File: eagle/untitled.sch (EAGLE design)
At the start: 38 parts, among them J1 JTAG, U1 MMA3202KEG

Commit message: Rework some labels.
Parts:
- Q1: value (none) -> 16MHz
- S1: value TAC_SWITCHSMD -> RESET
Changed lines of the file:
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@@
 <part name="R1" library="SparkFun-Passives" deviceset="RESISTOR" device="1206"/>
 <part name="R2" library="SparkFun-Passives" deviceset="RESISTOR" device="1206"/>
-<part name="S1" library="SparkFun-Retired" deviceset="TAC_SWITCH" device="SMD" value="TAC_SWITCHSMD"/>
+<part name="S1" library="SparkFun-Retired" deviceset="TAC_SWITCH" device="SMD" value="RESET"/>
 <part name="R3" library="SparkFun-Passives" deviceset="RESISTOR" device="1206" value="10k"/>
 <part name="GND-ISO1" library="SparkFun-Aesthetics" deviceset="GND-ISO" device=""/>
 <part name="GND-ISO2" library="SparkFun-Aesthetics" deviceset="GND-ISO" device=""/>
-<part name="Q1" library="special" deviceset="XTAL/S" device=""/>
+<part name="Q1" library="special" deviceset="XTAL/S" device="" value="16MHz"/>
 <part name="C1" library="capacitor-wima" deviceset="C" device="2.5/2"/>
 <part name="C2" library="capacitor-wima" deviceset="C" device="2.5/2"/>

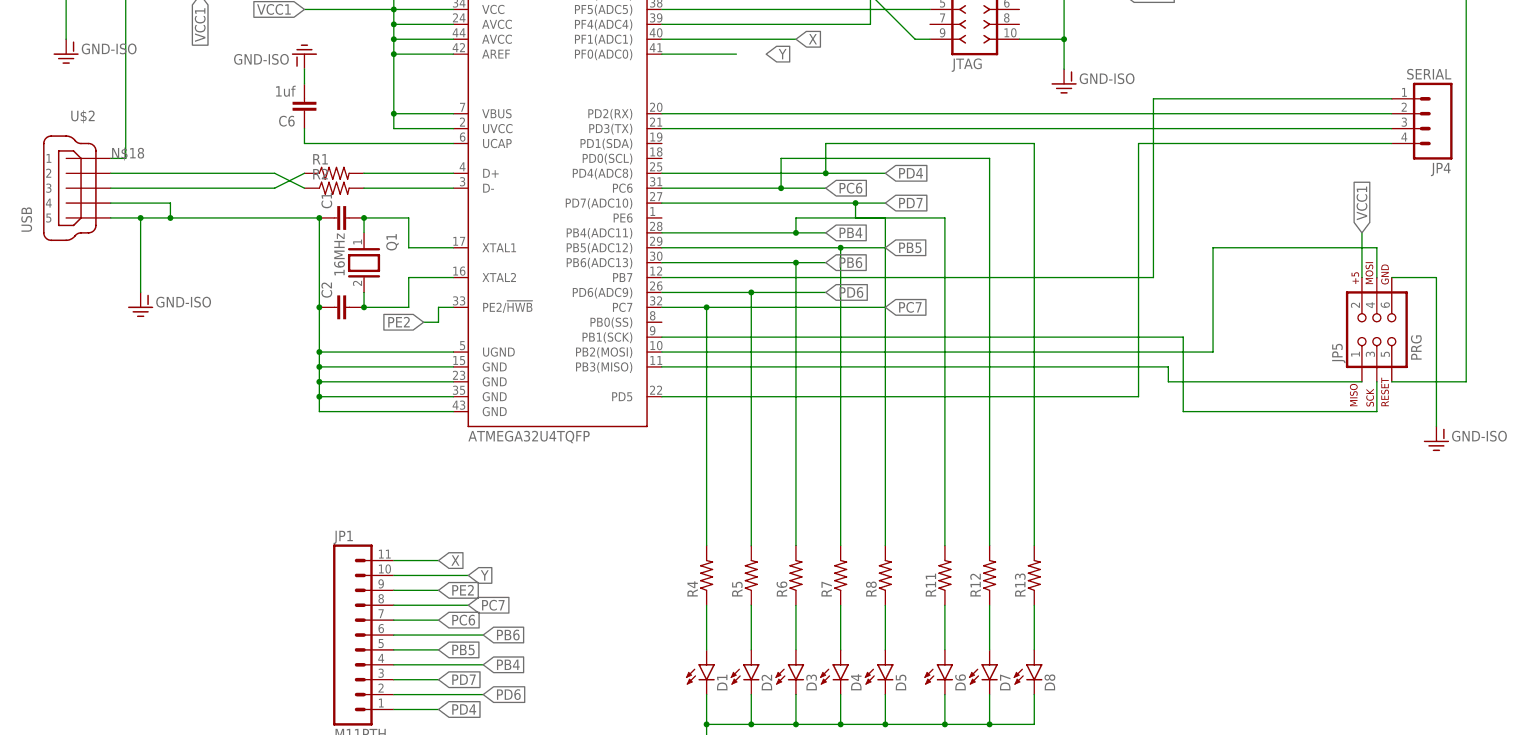
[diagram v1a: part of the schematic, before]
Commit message: Replace usb micro connector with mini type.
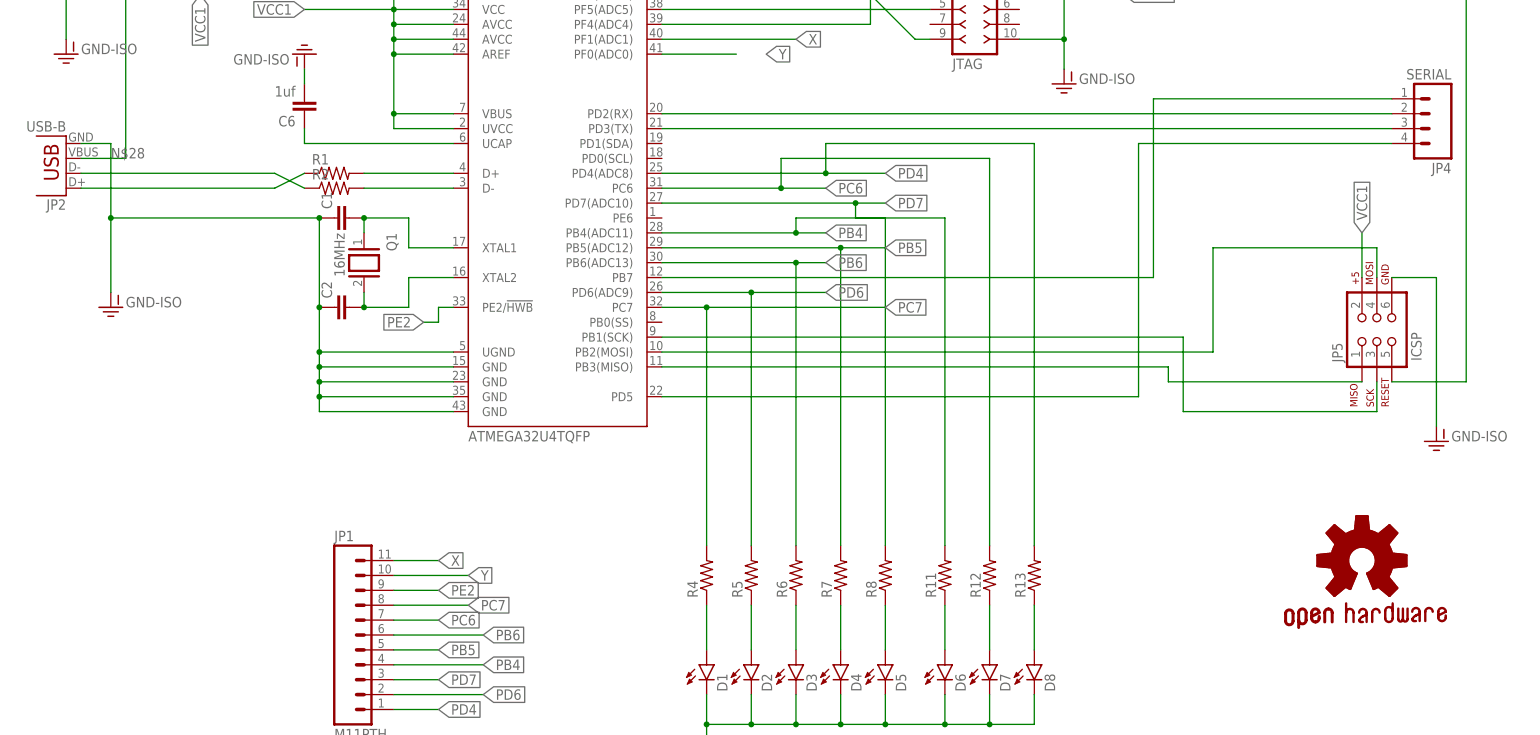
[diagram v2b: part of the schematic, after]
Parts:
- removed U$2: USB, con-hirose:MICRO-USB-ZX62R-B-5P
- added GOLD_ORB_SM1: OSHWLOGO_GOLD_ORB_SM, bfl:OSHWLOGO_GOLD_ORB_SM
- added JP2: USB-B, SparkFun-Connectors:USBPTH
- C6: device capacitor-wima:C2.5/2 -> eagle-ltspice:CC1206
- JP5: value PRG -> ICSP
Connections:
- removed net N$18: G1.+, SJ1.2, U$2.1
- new net N$28: G1.+, JP2.VBUS, SJ1.2
- net GND-ISO: now also JP2.GND; no longer U$2.4, U$2.5
- net N$3: now also JP2.D-; no longer U$2.2
- net N$4: now also JP2.D+; no longer U$2.3
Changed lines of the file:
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@@
 <parts>
 <part name="U$1" library="SparkFun-Retired" deviceset="ATMEGA32U4" device="TQFP"/>
-<part name="U$2" library="con-hirose" deviceset="MICRO-USB-" device="ZX62R-B-5P" value="USB"/>
 <part name="R1" library="SparkFun-Passives" deviceset="RESISTOR" device="1206"/>
 <part name="R2" library="SparkFun-Passives" deviceset="RESISTOR" device="1206"/>
@@
 <part name="GND-ISO6" library="SparkFun-Aesthetics" deviceset="GND-ISO" device=""/>
 <part name="GND-ISO7" library="SparkFun-Aesthetics" deviceset="GND-ISO" device=""/>
-<part name="C6" library="capacitor-wima" deviceset="C" device="2.5/2" value="1uf"/>
+<part name="C6" library="eagle-ltspice" deviceset="C" device="C1206" value="1uf"/>
 <part name="GND-ISO8" library="SparkFun-Aesthetics" deviceset="GND-ISO" device=""/>
 <part name="JP4" library="SparkFun-Connectors" deviceset="M04" device="LOCK_LONGPADS" value="SERIAL"/>
-<part name="JP5" library="SparkFun-Connectors" deviceset="AVR_SPI_PRG_6" device="PTH" value="PRG"/>
+<part name="JP5" library="SparkFun-Connectors" deviceset="AVR_SPI_PRG_6" device="PTH" value="ICSP"/>
 <part name="GND-ISO3" library="SparkFun-Aesthetics" deviceset="GND-ISO" device=""/>
 <part name="JP1" library="SparkFun-Connectors" deviceset="M11" device="PTH"/>
@@
 <part name="J1" library="con-headers-jp" deviceset="F-2X05-" device="DIL-2MM" value="JTAG"/>
 <part name="GND-ISO10" library="SparkFun-Aesthetics" deviceset="GND-ISO" device=""/>
+<part name="GOLD_ORB_SM1" library="bfl" deviceset="OSHWLOGO" device="_GOLD_ORB_SM"/>
+<part name="JP2" library="SparkFun-Connectors" deviceset="USB" device="PTH" value="USB-B"/>
 </parts>
 <sheets>
@@
 <instances>
 <instance part="U$1" gate="G$1" x="43.18" y="43.18"/>
-<instance part="U$2" gate="G$1" x="-38.1" y="43.18" rot="MR0"/>
 <instance part="R1" gate="G$1" x="5.08" y="45.72"/>
 <instance part="R2" gate="G$1" x="5.08" y="43.18"/>
@@
 <instance part="R3" gate="G$1" x="15.24" y="83.82" rot="R270"/>
 <instance part="GND-ISO1" gate="G$1" x="-5.08" y="86.36"/>
-<instance part="GND-ISO2" gate="G$1" x="-27.94" y="22.86"/>
+<instance part="GND-ISO2" gate="G$1" x="-33.02" y="22.86"/>
 <instance part="Q1" gate="G$1" x="10.16" y="30.48" rot="R270"/>
 <instance part="C1" gate="G$1" x="5.08" y="38.1" rot="R90"/>
@@
 <instance part="J1" gate="G$1" x="114.3" y="73.66"/>
 <instance part="GND-ISO10" gate="G$1" x="129.54" y="60.96"/>
+<instance part="GOLD_ORB_SM1" gate="G$1" x="180.34" y="-20.32"/>
+<instance part="JP2" gate="G$1" x="-40.64" y="50.8" rot="R180"/>
 </instances>
 <busses>
@@
 <net name="N$3" class="0">
 <segment>
-<pinref part="U$2" gate="G$1" pin="2"/>
-<wire x1="-33.02" y1="45.72" x2="-5.08" y2="45.72" width="0.1524" layer="91"/>
+<wire x1="-38.1" y1="45.72" x2="-5.08" y2="45.72" width="0.1524" layer="91"/>
 <wire x1="-5.08" y1="45.72" x2="0" y2="43.18" width="0.1524" layer="91"/>
 <pinref part="R2" gate="G$1" pin="1"/>
+<pinref part="JP2" gate="G$1" pin="D-"/>
 </segment>
 </net>
 <net name="N$4" class="0">
 <segment>
-<pinref part="U$2" gate="G$1" pin="3"/>
-<wire x1="-33.02" y1="43.18" x2="-5.08" y2="43.18" width="0.1524" layer="91"/>
+<wire x1="-38.1" y1="43.18" x2="-5.08" y2="43.18" width="0.1524" layer="91"/>
 <wire x1="-5.08" y1="43.18" x2="0" y2="45.72" width="0.1524" layer="91"/>
 <pinref part="R1" gate="G$1" pin="1"/>
+<pinref part="JP2" gate="G$1" pin="D+"/>
 </segment>
 </net>
@@
 </segment>
 <segment>
-<pinref part="U$2" gate="G$1" pin="5"/>
-<wire x1="-33.02" y1="38.1" x2="-27.94" y2="38.1" width="0.1524" layer="91"/>
-<wire x1="-27.94" y1="38.1" x2="-22.86" y2="38.1" width="0.1524" layer="91"/>
-<wire x1="-22.86" y1="38.1" x2="2.54" y2="38.1" width="0.1524" layer="91"/>
+<wire x1="-33.02" y1="38.1" x2="2.54" y2="38.1" width="0.1524" layer="91"/>
 <wire x1="2.54" y1="38.1" x2="2.54" y2="22.86" width="0.1524" layer="91"/>
 <pinref part="U$1" gate="G$1" pin="UGND"/>
 <wire x1="2.54" y1="22.86" x2="2.54" y2="15.24" width="0.1524" layer="91"/>
 <wire x1="2.54" y1="15.24" x2="25.4" y2="15.24" width="0.1524" layer="91"/>
-<pinref part="U$2" gate="G$1" pin="4"/>
-<wire x1="-33.02" y1="40.64" x2="-22.86" y2="40.64" width="0.1524" layer="91"/>
-<wire x1="-22.86" y1="40.64" x2="-22.86" y2="38.1" width="0.1524" layer="91"/>
-<junction x="-22.86" y="38.1"/>
 <pinref part="GND-ISO2" gate="G$1" pin="GND-ISO"/>
-<wire x1="-27.94" y1="25.4" x2="-27.94" y2="38.1" width="0.1524" layer="91"/>
-<junction x="-27.94" y="38.1"/>
+<junction x="-33.02" y="38.1"/>
 <pinref part="U$1" gate="G$1" pin="GND@43"/>
+<wire x1="-33.02" y1="25.4" x2="-33.02" y2="38.1" width="0.1524" layer="91"/>
 <wire x1="25.4" y1="5.08" x2="2.54" y2="5.08" width="0.1524" layer="91"/>
 <wire x1="2.54" y1="5.08" x2="2.54" y2="7.62" width="0.1524" layer="91"/>
@@
 <pinref part="C2" gate="G$1" pin="1"/>
 <junction x="2.54" y="22.86"/>
+<pinref part="JP2" gate="G$1" pin="GND"/>
+<wire x1="-38.1" y1="50.8" x2="-33.02" y2="50.8" width="0.1524" layer="91"/>
+<wire x1="-33.02" y1="50.8" x2="-33.02" y2="38.1" width="0.1524" layer="91"/>
 </segment>
 <segment>
@@
 </segment>
 </net>
-<net name="N$18" class="0">
-<segment>
-<pinref part="U$2" gate="G$1" pin="1"/>
-<wire x1="-33.02" y1="48.26" x2="-30.48" y2="48.26" width="0.1524" layer="91"/>
-<label x="-33.02" y="48.26" size="1.778" layer="95"/>
-<pinref part="SJ1" gate="G$1" pin="2"/>
-<wire x1="-30.48" y1="48.26" x2="-30.48" y2="88.9" width="0.1524" layer="91"/>
-<wire x1="-30.48" y1="88.9" x2="-22.86" y2="88.9" width="0.1524" layer="91"/>
-<pinref part="G1" gate="G$1" pin="+"/>
-<wire x1="-30.48" y1="88.9" x2="-40.64" y2="88.9" width="0.1524" layer="91"/>
-<junction x="-30.48" y="88.9"/>
-</segment>
-</net>
 <net name="VCC1" class="0">
 <segment>
@@
 </segment>
 </net>
+<net name="N$28" class="0">
+<segment>
+<pinref part="G1" gate="G$1" pin="+"/>
+<pinref part="SJ1" gate="G$1" pin="2"/>
+<wire x1="-30.48" y1="88.9" x2="-22.86" y2="88.9" width="0.1524" layer="91"/>
+<wire x1="-30.48" y1="88.9" x2="-40.64" y2="88.9" width="0.1524" layer="91"/>
+<junction x="-30.48" y="88.9"/>
+<wire x1="-30.48" y1="48.26" x2="-30.48" y2="88.9" width="0.1524" layer="91"/>
+<label x="-33.02" y="48.26" size="1.778" layer="95"/>
+<pinref part="JP2" gate="G$1" pin="VBUS"/>
+<wire x1="-30.48" y1="48.26" x2="-38.1" y2="48.26" width="0.1524" layer="91"/>
+</segment>
+</net>

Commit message: Update eagle files.
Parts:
- added D10, D11, D12: DIODE, gipi:DIODE
- C1, C2, C3, C4, C5: device capacitor-wima:C2.5/2 -> SparkFun-Capacitors:CAP1206
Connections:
- new net N$32: D10.A, JP2.VBUS
- new net N$33: D11.A, G1.+
- new net N$34: D12.A, JP5.2
- net N$28: now also D10.C, D11.C; no longer G1.+, JP2.VBUS
- net VCC1: now also D12.C; no longer JP5.2
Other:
- moved on the sheet: C1, C2, C3, C4, C5
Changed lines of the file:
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@@
 <part name="GND-ISO2" library="SparkFun-Aesthetics" deviceset="GND-ISO" device=""/>
 <part name="Q1" library="special" deviceset="XTAL/S" device="" value="16MHz"/>
-<part name="C1" library="capacitor-wima" deviceset="C" device="2.5/2"/>
-<part name="C2" library="capacitor-wima" deviceset="C" device="2.5/2"/>
+<part name="C1" library="SparkFun-Capacitors" deviceset="CAP" device="1206"/>
+<part name="C2" library="SparkFun-Capacitors" deviceset="CAP" device="1206"/>
 <part name="U1" library="gipi" deviceset="MMA3202KEG" device=""/>
 <part name="G1" library="battery" deviceset="10MM_SM_COIN_CELL_CLIP" device="" value="BAT"/>
 <part name="GND-ISO4" library="SparkFun-Aesthetics" deviceset="GND-ISO" device=""/>
-<part name="C3" library="capacitor-wima" deviceset="C" device="2.5/2"/>
+<part name="C3" library="SparkFun-Capacitors" deviceset="CAP" device="1206"/>
 <part name="SJ1" library="SparkFun-Retired" deviceset="SOLDERJUMPER_2WAY" device="PASTE2&amp;3"/>
 <part name="GND-ISO5" library="SparkFun-Aesthetics" deviceset="GND-ISO" device=""/>
 <part name="R9" library="SparkFun-Passives" deviceset="RESISTOR" device="1206" value="10k"/>
 <part name="R10" library="SparkFun-Passives" deviceset="RESISTOR" device="1206" value="10k"/>
-<part name="C4" library="capacitor-wima" deviceset="C" device="2.5/2"/>
-<part name="C5" library="capacitor-wima" deviceset="C" device="2.5/2"/>
+<part name="C4" library="SparkFun-Capacitors" deviceset="CAP" device="1206"/>
+<part name="C5" library="SparkFun-Capacitors" deviceset="CAP" device="1206"/>
 <part name="GND-ISO6" library="SparkFun-Aesthetics" deviceset="GND-ISO" device=""/>
 <part name="GND-ISO7" library="SparkFun-Aesthetics" deviceset="GND-ISO" device=""/>
@@
 <part name="GOLD_ORB_SM1" library="bfl" deviceset="OSHWLOGO" device="_GOLD_ORB_SM"/>
 <part name="JP2" library="SparkFun-Connectors" deviceset="USB" device="PTH" value="USB-B"/>
+<part name="D10" library="gipi" deviceset="DIODE" device=""/>
+<part name="D11" library="gipi" deviceset="DIODE" device=""/>
+<part name="D12" library="gipi" deviceset="DIODE" device=""/>
 </parts>
 <sheets>
@@
 <instance part="GOLD_ORB_SM1" gate="G$1" x="180.34" y="-20.32"/>
 <instance part="JP2" gate="G$1" x="-40.64" y="50.8" rot="R180"/>
+<instance part="D10" gate="G$1" x="-30.48" y="73.66" rot="R90"/>
+<instance part="D11" gate="G$1" x="-35.56" y="88.9"/>
+<instance part="D12" gate="G$1" x="185.42" y="40.64"/>
 </instances>
 <busses>
@@
 </segment>
 <segment>
-<wire x1="-33.02" y1="38.1" x2="2.54" y2="38.1" width="0.1524" layer="91"/>
-<wire x1="2.54" y1="38.1" x2="2.54" y2="22.86" width="0.1524" layer="91"/>
+<wire x1="-33.02" y1="38.1" x2="0" y2="38.1" width="0.1524" layer="91"/>
+<wire x1="0" y1="38.1" x2="0" y2="22.86" width="0.1524" layer="91"/>
 <pinref part="U$1" gate="G$1" pin="UGND"/>
-<wire x1="2.54" y1="22.86" x2="2.54" y2="15.24" width="0.1524" layer="91"/>
+<wire x1="0" y1="22.86" x2="2.54" y2="15.24" width="0.1524" layer="91"/>
 <wire x1="2.54" y1="15.24" x2="25.4" y2="15.24" width="0.1524" layer="91"/>
 <pinref part="GND-ISO2" gate="G$1" pin="GND-ISO"/>
@@
 <junction x="2.54" y="7.62"/>
 <pinref part="C1" gate="G$1" pin="1"/>
-<junction x="2.54" y="38.1"/>
+<junction x="0" y="38.1"/>
 <pinref part="C2" gate="G$1" pin="1"/>
-<junction x="2.54" y="22.86"/>
+<junction x="0" y="22.86"/>
 <pinref part="JP2" gate="G$1" pin="GND"/>
 <wire x1="-38.1" y1="50.8" x2="-33.02" y2="50.8" width="0.1524" layer="91"/>
@@
 <pinref part="C5" gate="G$1" pin="1"/>
 <pinref part="GND-ISO6" gate="G$1" pin="GND-ISO"/>
+<wire x1="116.84" y1="-157.48" x2="116.84" y2="-160.02" width="0.1524" layer="91"/>
 </segment>
 <segment>
 <pinref part="C4" gate="G$1" pin="1"/>
 <pinref part="GND-ISO7" gate="G$1" pin="GND-ISO"/>
+<wire x1="137.16" y1="-157.48" x2="137.16" y2="-160.02" width="0.1524" layer="91"/>
 </segment>
 <segment>
@@
 <junction x="38.1" y="-149.86"/>
 <wire x1="38.1" y1="-149.86" x2="20.32" y2="-149.86" width="0.1524" layer="91"/>
-<wire x1="20.32" y1="-149.86" x2="20.32" y2="-147.32" width="0.1524" layer="91"/>
 <pinref part="GND-ISO4" gate="G$1" pin="GND-ISO"/>
 <wire x1="38.1" y1="-187.96" x2="38.1" y2="-154.94" width="0.1524" layer="91"/>
@@
 <pinref part="Q1" gate="G$1" pin="2"/>
 <pinref part="C2" gate="G$1" pin="2"/>
-<wire x1="10.16" y1="25.4" x2="10.16" y2="22.86" width="0.1524" layer="91"/>
+<wire x1="10.16" y1="25.4" x2="7.62" y2="22.86" width="0.1524" layer="91"/>
 <wire x1="17.78" y1="27.94" x2="17.78" y2="22.86" width="0.1524" layer="91"/>
-<wire x1="17.78" y1="22.86" x2="10.16" y2="22.86" width="0.1524" layer="91"/>
-<junction x="10.16" y="22.86"/>
+<wire x1="17.78" y1="22.86" x2="7.62" y2="22.86" width="0.1524" layer="91"/>
+<junction x="7.62" y="22.86"/>
 </segment>
 </net>
@@
 <segment>
 <pinref part="C1" gate="G$1" pin="2"/>
-<wire x1="10.16" y1="38.1" x2="17.78" y2="38.1" width="0.1524" layer="91"/>
+<wire x1="7.62" y1="38.1" x2="17.78" y2="38.1" width="0.1524" layer="91"/>
 <wire x1="17.78" y1="38.1" x2="17.78" y2="33.02" width="0.1524" layer="91"/>
 <pinref part="U$1" gate="G$1" pin="XTAL1"/>
 <wire x1="25.4" y1="33.02" x2="17.78" y2="33.02" width="0.1524" layer="91"/>
 <pinref part="Q1" gate="G$1" pin="1"/>
-<wire x1="10.16" y1="38.1" x2="10.16" y2="35.56" width="0.1524" layer="91"/>
-<junction x="10.16" y="38.1"/>
+<wire x1="7.62" y1="38.1" x2="10.16" y2="35.56" width="0.1524" layer="91"/>
+<junction x="7.62" y="38.1"/>
 </segment>
 </net>
@@
 </segment>
 <segment>
-<pinref part="JP5" gate="G$1" pin="2"/>
-<wire x1="180.34" y1="27.94" x2="180.34" y2="35.56" width="0.1524" layer="91"/>
-<label x="180.34" y="35.56" size="1.778" layer="95" rot="R90" xref="yes"/>
-</segment>
-<segment>
 <pinref part="J1" gate="G$1" pin="4"/>
 <wire x1="121.92" y1="76.2" x2="139.7" y2="76.2" width="0.1524" layer="91"/>
 <label x="139.7" y="76.2" size="1.778" layer="95" xref="yes"/>
 </segment>
+<segment>
+<pinref part="D12" gate="G$1" pin="C"/>
+<wire x1="187.96" y1="40.64" x2="203.2" y2="40.64" width="0.1524" layer="91"/>
+<label x="203.2" y="40.64" size="1.778" layer="95" xref="yes"/>
+</segment>
 </net>
 <net name="VCC2" class="0">
@@
 <pinref part="U1" gate="G$1" pin="VCC"/>
 <wire x1="48.26" y1="-139.7" x2="35.56" y2="-139.7" width="0.1524" layer="91"/>
-<wire x1="35.56" y1="-139.7" x2="20.32" y2="-139.7" width="0.1524" layer="91"/>
-<wire x1="20.32" y1="-139.7" x2="20.32" y2="-129.54" width="0.1524" layer="91"/>
+<wire x1="35.56" y1="-139.7" x2="20.32" y2="-142.24" width="0.1524" layer="91"/>
+<wire x1="20.32" y1="-142.24" x2="20.32" y2="-129.54" width="0.1524" layer="91"/>
 <pinref part="C3" gate="G$1" pin="2"/>
-<junction x="20.32" y="-139.7"/>
+<junction x="20.32" y="-142.24"/>
 <label x="20.32" y="-129.54" size="1.778" layer="95" rot="R90" xref="yes"/>
 <pinref part="U1" gate="G$1" pin="AVCC"/>
@@
 <wire x1="106.68" y1="-144.78" x2="137.16" y2="-144.78" width="0.1524" layer="91"/>
 <pinref part="C4" gate="G$1" pin="2"/>
-<wire x1="137.16" y1="-144.78" x2="137.16" y2="-149.86" width="0.1524" layer="91"/>
+<wire x1="137.16" y1="-144.78" x2="137.16" y2="-152.4" width="0.1524" layer="91"/>
 <wire x1="137.16" y1="-144.78" x2="144.78" y2="-144.78" width="0.1524" layer="91"/>
 <junction x="137.16" y="-144.78"/>
@@
 <wire x1="106.68" y1="-139.7" x2="116.84" y2="-139.7" width="0.1524" layer="91"/>
 <pinref part="C5" gate="G$1" pin="2"/>
-<wire x1="116.84" y1="-139.7" x2="116.84" y2="-149.86" width="0.1524" layer="91"/>
+<wire x1="116.84" y1="-139.7" x2="116.84" y2="-152.4" width="0.1524" layer="91"/>
 <junction x="116.84" y="-139.7"/>
 <wire x1="116.84" y1="-139.7" x2="144.78" y2="-139.7" width="0.1524" layer="91"/>
@@
 <net name="N$28" class="0">
 <segment>
-<pinref part="G1" gate="G$1" pin="+"/>
 <pinref part="SJ1" gate="G$1" pin="2"/>
-<wire x1="-30.48" y1="88.9" x2="-22.86" y2="88.9" width="0.1524" layer="91"/>
-<wire x1="-30.48" y1="88.9" x2="-40.64" y2="88.9" width="0.1524" layer="91"/>
+<wire x1="-22.86" y1="88.9" x2="-30.48" y2="88.9" width="0.1524" layer="91"/>
+<pinref part="D10" gate="G$1" pin="C"/>
+<wire x1="-30.48" y1="76.2" x2="-30.48" y2="88.9" width="0.1524" layer="91"/>
+<pinref part="D11" gate="G$1" pin="C"/>
+<wire x1="-33.02" y1="88.9" x2="-30.48" y2="88.9" width="0.1524" layer="91"/>
 <junction x="-30.48" y="88.9"/>
-<wire x1="-30.48" y1="48.26" x2="-30.48" y2="88.9" width="0.1524" layer="91"/>
-<label x="-33.02" y="48.26" size="1.778" layer="95"/>
+</segment>
+</net>
+<net name="N$32" class="0">
+<segment>
 <pinref part="JP2" gate="G$1" pin="VBUS"/>
 <wire x1="-30.48" y1="48.26" x2="-38.1" y2="48.26" width="0.1524" layer="91"/>
-</segment>
-</net>
+<label x="-33.02" y="48.26" size="1.778" layer="95"/>
+<pinref part="D10" gate="G$1" pin="A"/>
+<wire x1="-30.48" y1="48.26" x2="-30.48" y2="71.12" width="0.1524" layer="91"/>
+</segment>
+</net>
+<net name="N$33" class="0">
+<segment>
+<pinref part="G1" gate="G$1" pin="+"/>
+<pinref part="D11" gate="G$1" pin="A"/>
+<wire x1="-40.64" y1="88.9" x2="-38.1" y2="88.9" width="0.1524" layer="91"/>
+</segment>
+</net>
+<net name="N$34" class="0">
+<segment>
+<pinref part="JP5" gate="G$1" pin="2"/>
+<wire x1="180.34" y1="27.94" x2="180.34" y2="40.64" width="0.1524" layer="91"/>
+<wire x1="180.34" y1="40.64" x2="182.88" y2="40.64" width="0.1524" layer="91"/>
+<pinref part="D12" gate="G$1" pin="A"/>
+</segment>
+</net>
